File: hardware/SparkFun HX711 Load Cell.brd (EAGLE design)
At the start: 30.5 x 22.9 mm, 25 parts, among them Q1 MMBT4403, U1 HX711

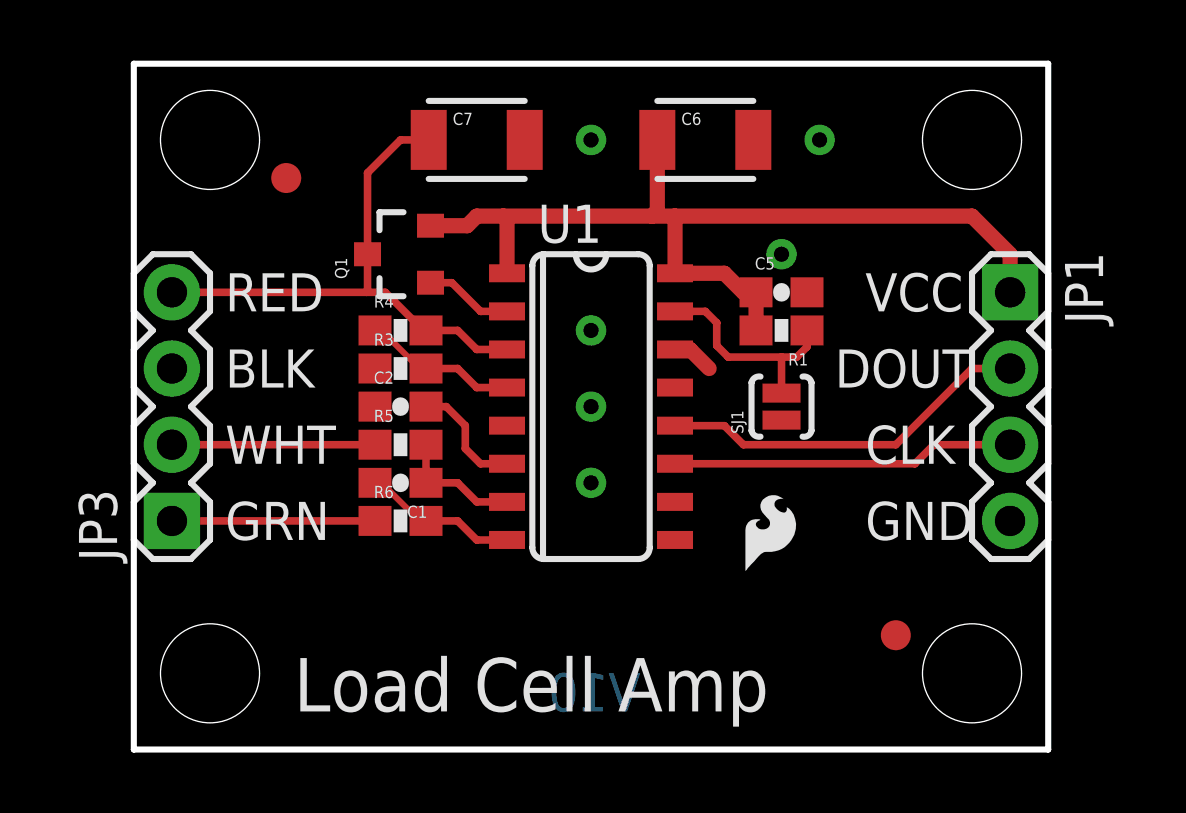
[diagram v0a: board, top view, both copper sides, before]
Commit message: Changes from initial QC checklist. Adding datasheet.
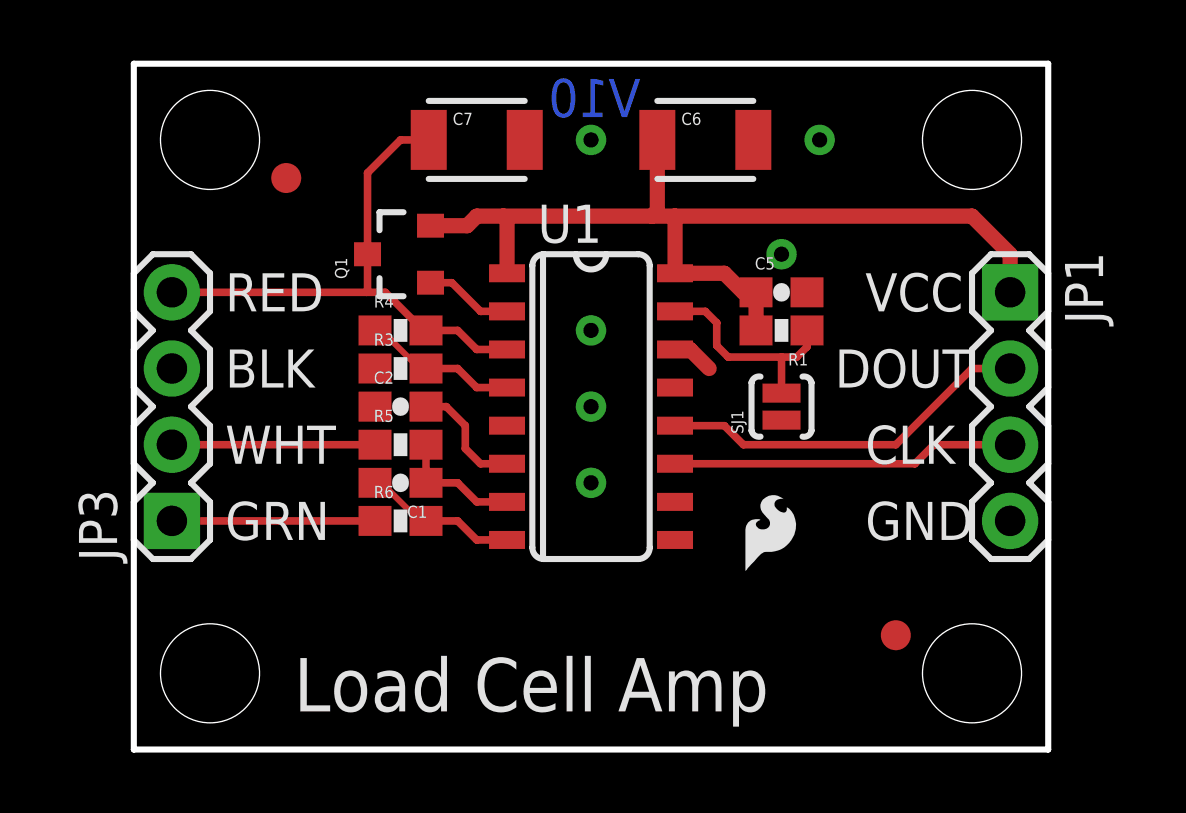
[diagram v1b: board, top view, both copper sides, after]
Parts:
- U1: device HX711:SO16 -> Testing:SO16
- renumbered U$7 to U7
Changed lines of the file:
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@@
 <?xml version="1.0" encoding="utf-8"?>
 <!DOCTYPE eagle SYSTEM "eagle.dtd">
-<eagle version="6.5.0">
+<eagle version="7.1.0">
 <drawing>
 <settings>
@@
 <layer number="251" name="SMDround" color="12" fill="11" visible="no" active="no"/>
 <layer number="254" name="cooling" color="7" fill="1" visible="no" active="yes"/>
+<layer number="255" name="routoute" color="7" fill="1" visible="no" active="yes"/>
 </layers>
 <board>
@@
 <text x="9.398" y="12.065" size="1.27" layer="22" font="vector" ratio="15" rot="MR0">BLK/E-</text>
 <text x="9.398" y="14.605" size="1.27" layer="22" font="vector" ratio="15" rot="MR0">RED/E+</text>
-<text x="16.891" y="1.27" size="1.27" layer="16" font="vector" ratio="20" rot="MR0">V10</text>
+<text x="16.891" y="21.082" size="1.27" layer="16" font="vector" ratio="20" rot="MR0">V10</text>
 <text x="24.384" y="6.985" size="1.27" layer="21" font="vector" ratio="15">GND</text>
 <text x="23.368" y="12.065" size="1.27" layer="21" font="vector" ratio="15">DOUT</text>
@@
 <text x="30.48" y="-21.59" size="1.778" layer="51" font="vector" ratio="15">N. Seidle</text>
 <text x="25.146" y="1.27" size="1.778" layer="22" font="vector" ratio="15" rot="MR0">Load Cell Amp</text>
+<dimension x1="30.48" y1="22.86" x2="0" y2="22.86" x3="15.24" y3="31.75" textsize="1.778" textratio="15" layer="47" unit="inch"/>
+<dimension x1="0" y1="0" x2="0" y2="22.86" x3="-5.08" y3="11.43" textsize="1.778" textratio="15" layer="47" unit="inch"/>
+<dimension x1="27.94" y1="20.32" x2="27.94" y2="2.54" x3="35.56" y3="11.43" textsize="1.778" textratio="15" layer="47" unit="inch"/>
+<dimension x1="27.94" y1="2.54" x2="2.54" y2="2.54" x3="15.24" y3="-5.08" textsize="1.778" textratio="15" layer="47" unit="inch"/>
+<dimension x1="1.27" y1="15.24" x2="29.21" y2="15.24" x3="15.24" y3="27.94" textsize="1.778" textratio="15" layer="47" unit="inch"/>
+<dimension x1="1.27" y1="7.62" x2="1.27" y2="0" x3="-7.62" y3="3.81" textsize="1.778" textratio="15" layer="47" unit="inch"/>
 </plain>
 <attributes>
@@
 <pass name="Default">
 <param name="RoutingGrid" value="50mil"/>
+<param name="AutoGrid" value="1"/>
+<param name="Efforts" value="0"/>
+<param name="TopRouterVariant" value="1"/>
 <param name="tpViaShape" value="round"/>
 <param name="PrefDir.1" value="|"/>
@@
 </autorouter>
 <elements>
-<element name="U$7" library="SparkFun-Aesthetics" package="OSHW-LOGO-S" value="OSHW-LOGOS" x="6.35" y="20.32" rot="MR0"/>
+<element name="U7" library="SparkFun-Aesthetics" package="OSHW-LOGO-S" value="OSHW-LOGOS" x="6.35" y="20.32" rot="MR0"/>
 <element name="FRAME1" library="SparkFun-Aesthetics" package="CREATIVE_COMMONS" value="FRAME-LETTER" x="-0.65105625" y="-21.59"/>
 <element name="STANDOFF1" library="SparkFun-Electromechanical" package="STAND-OFF" value="STAND-OFF" x="2.54" y="2.54"/>
@@
 <element name="LOGO1" library="SparkFun-Aesthetics" package="SFE_LOGO_NAME_FLAME_.1" value="SFE_LOGO_NAME_FLAME.1_INCH" x="21.082" y="4.191" rot="MR0"/>
 <element name="JP1" library="SparkFun-Connectors" package="1X04" value="" x="29.21" y="15.24" rot="R270"/>
-<element name="U1" library="HX711" package="SO16" value="HX711" x="15.24" y="11.43" rot="R270"/>
+<element name="U1" library="Testing" package="SO16" value="HX711" x="15.24" y="11.43" rot="R270">
+<attribute name="PROD_ID" value="IC-12445" x="15.24" y="11.43" size="1.778" layer="27" rot="R270" display="off"/>
+<attribute name="VALUE" value="HX711" x="15.24" y="11.43" size="1.778" layer="27" rot="R270" display="off"/>
+</element>
 <element name="Q1" library="SparkFun-DiscreteSemi" package="SOT23-3" value="MMBT4403" x="8.89" y="16.51" rot="R90">
 <attribute name="PROD_ID" value="TRANS-09245" x="8.89" y="16.51" size="1.778" layer="27" font="vector" ratio="15" rot="R90" display="off"/>

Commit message: Spread out 0603 components and fixed silk. See issue 1.
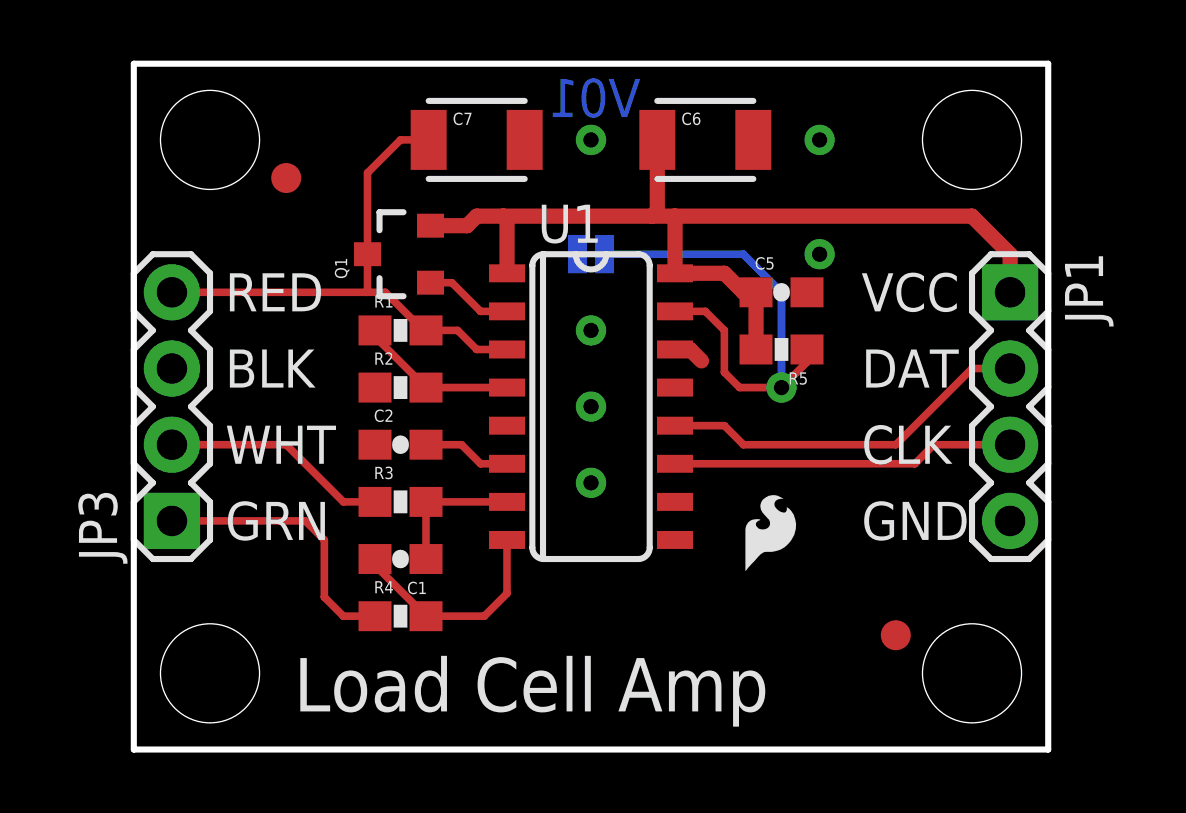
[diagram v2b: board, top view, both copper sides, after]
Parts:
- removed R6: 100, SparkFun-Resistors:0603-RES
- added R2: 10K, SparkFun-Resistors:0603-RES
- R3, R4: value 10K -> 100
- R5: value 100 -> 10K
- moved R5 13.1 mm to (21.6, 13.3), turned to 180 degrees
- moved R1 12.7 mm to (8.89, 14.0), turned to 0 degrees
- moved R4 9.53 mm to (8.89, 4.45)
- moved SJ1 8.13 mm to (15.2, 16.5), flipped to the bottom, turned to 180 degrees
- moved R3 4.44 mm to (8.89, 8.26)
- moved C1 2.54 mm to (8.89, 6.35)
- moved C2 1.27 mm to (8.89, 10.2)
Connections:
- net DOUT renamed DAT
- net A+: now also R4.1; no longer R6.1
- net A-: now also R3.1; no longer R5.1
- net AVDD: now also R1.2; no longer R4.2
- net GND: now also R2.1; no longer R3.1
- net N$1: now also R5.1; no longer R1.1
- net N$2: now also R3.2; no longer R5.2
- net N$3: now also R4.2; no longer R6.2
- net N$6: now also R1.1, R2.2; no longer R3.2, R4.1
- net VCC: now also R5.2; no longer R1.2
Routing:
- net N$1: track 7.37 -> 16.6 mm, vias 0 -> 1
- net A+: track 6.77 -> 9.20 mm
- net N$3: track 5.19 -> 7.41 mm
- net N$7: track 3.94 -> 2.96 mm
- net A-: track 6.77 -> 7.56 mm
- net VCC: track 32.0 -> 32.6 mm
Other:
- board text added: "DAT"
- board text added: "RATE"
- board text added: "V01"
- board text removed: "DOUT"
- board text removed: "V10"

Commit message: Broke out channel B. Adjusted some traces.
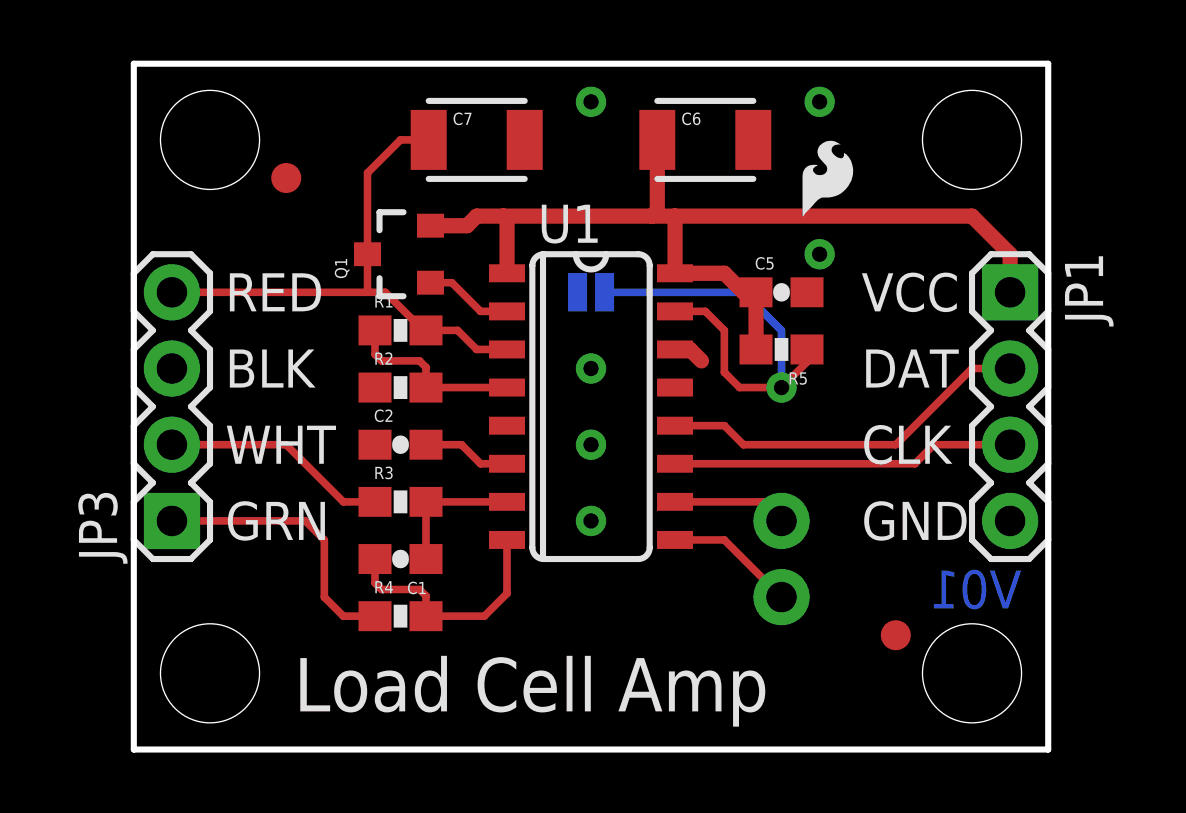
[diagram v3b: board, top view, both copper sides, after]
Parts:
- added JP2: M02PTH, SparkFun-Connectors:1X02
- moved LOGO1 13.0 mm to (21.0, 17.1)
- moved LOGO3 12.0 mm to (22.0, 17.4)
- moved SJ1 1.27 mm to (15.2, 15.2)
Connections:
- new net B+: JP2.1, U1.10
- new net B-: JP2.2, U1.9
- net GND: no longer U1.10, U1.9
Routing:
- net B-: track 0.00 -> 4.34 mm
- net B+: track 0.00 -> 3.81 mm
- net N$1: track 16.6 -> 15.4 mm
- net N$6: track 5.31 -> 6.05 mm
- net N$3: track 7.41 -> 8.15 mm
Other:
- board text added: "B+"
- board text added: "B-"
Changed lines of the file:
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@@
 <?xml version="1.0" encoding="utf-8"?>
 <!DOCTYPE eagle SYSTEM "eagle.dtd">
-<eagle version="6.5.0">
+<eagle version="7.1.0">
 <drawing>
 <settings>
@@
 <layer number="56" name="wert" color="7" fill="1" visible="no" active="no"/>
 <layer number="57" name="tCAD" color="7" fill="1" visible="no" active="no"/>
+<layer number="90" name="Modules" color="5" fill="1" visible="no" active="no"/>
 <layer number="91" name="Nets" color="2" fill="1" visible="no" active="no"/>
 <layer number="92" name="Busses" color="1" fill="1" visible="no" active="no"/>
@@
 <text x="9.398" y="12.065" size="1.27" layer="22" font="vector" ratio="15" rot="MR0">BLK/E-</text>
 <text x="9.398" y="14.605" size="1.27" layer="22" font="vector" ratio="15" rot="MR0">RED/E+</text>
-<text x="16.891" y="21.082" size="1.27" layer="16" font="vector" ratio="20" rot="MR0">V01</text>
+<text x="29.591" y="4.699" size="1.27" layer="16" font="vector" ratio="20" rot="MR0">V01</text>
 <text x="24.257" y="6.985" size="1.27" layer="21" font="vector" ratio="15">GND</text>
 <text x="24.257" y="12.065" size="1.27" layer="21" font="vector" ratio="15">DAT</text>
@@
 <dimension x1="1.27" y1="15.24" x2="29.21" y2="15.24" x3="15.24" y3="27.94" textsize="1.778" textratio="15" layer="47" unit="inch"/>
 <dimension x1="1.27" y1="7.62" x2="1.27" y2="0" x3="-7.62" y3="3.81" textsize="1.778" textratio="15" layer="47" unit="inch"/>
-<text x="20.955" y="15.875" size="1.27" layer="22" font="vector" ratio="15" rot="MR0">RATE</text>
+<text x="20.955" y="14.605" size="1.27" layer="22" font="vector" ratio="15" rot="MR0">RATE</text>
+<text x="19.685" y="6.985" size="1.27" layer="22" font="vector" ratio="15" rot="MR0">B+</text>
+<text x="19.685" y="4.445" size="1.27" layer="22" font="vector" ratio="15" rot="MR0">B-</text>
 </plain>
 <attributes>
@@
 <pass name="Default">
 <param name="RoutingGrid" value="50mil"/>
+<param name="AutoGrid" value="1"/>
+<param name="Efforts" value="0"/>
+<param name="TopRouterVariant" value="1"/>
 <param name="tpViaShape" value="round"/>
 <param name="PrefDir.1" value="|"/>
@@
 <element name="STANDOFF3" library="SparkFun-Electromechanical" package="STAND-OFF" value="STAND-OFF" x="2.54" y="20.32"/>
 <element name="STANDOFF4" library="SparkFun-Electromechanical" package="STAND-OFF" value="STAND-OFF" x="27.94" y="20.32"/>
-<element name="LOGO1" library="SparkFun-Aesthetics" package="SFE_LOGO_NAME_FLAME_.1" value="SFE_LOGO_NAME_FLAME.1_INCH" x="21.082" y="4.191" rot="MR0"/>
+<element name="LOGO1" library="SparkFun-Aesthetics" package="SFE_LOGO_NAME_FLAME_.1" value="SFE_LOGO_NAME_FLAME.1_INCH" x="20.955" y="17.145" rot="MR0"/>
 <element name="JP1" library="SparkFun-Connectors" package="1X04" value="" x="29.21" y="15.24" rot="R270"/>
 <element name="U1" library="Testing" package="SO16" value="HX711" x="15.24" y="11.43" rot="R270">
@@
 <attribute name="PROD_ID" value="RES-00824" x="21.59" y="13.335" size="1.778" layer="27" font="vector" ratio="15" rot="R180" display="off"/>
 </element>
-<element name="SJ1" library="SparkFun-Passives" package="PAD-JUMPER-2-NO_YES_SILK" value="" x="15.24" y="16.51" rot="MR180"/>
+<element name="SJ1" library="SparkFun-Passives" package="PAD-JUMPER-2-NO_YES_SILK" value="" x="15.24" y="15.24" rot="MR180"/>
 <element name="C1" library="SparkFun-Capacitors" package="0603-CAP" value="0.1uF" x="8.89" y="6.35" rot="R180">
 <attribute name="PROD_ID" value="CAP-08604" x="8.89" y="6.35" size="1.778" layer="27" font="vector" ratio="15" rot="R180" display="off"/>
@@
 <attribute name="PROD_ID" value="CAP-08604" x="8.89" y="10.16" size="1.778" layer="27" font="vector" ratio="15" display="off"/>
 </element>
-<element name="LOGO3" library="SparkFun-Aesthetics" package="SFE_LOGO_FLAME_.1" value="SFE_LOGO_FLAME.1_INCH" x="20.066" y="5.588"/>
+<element name="LOGO3" library="SparkFun-Aesthetics" package="SFE_LOGO_FLAME_.1" value="SFE_LOGO_FLAME.1_INCH" x="21.971" y="17.399"/>
 <element name="FID1" library="SparkFun-Aesthetics" package="FIDUCIAL-1X2" value="FIDUCIAL1X2" x="5.08" y="19.05"/>
 <element name="FID2" library="SparkFun-Aesthetics" package="FIDUCIAL-1X2" value="FIDUCIAL1X2" x="25.4" y="3.81"/>
+<element name="JP2" library="SparkFun-Connectors" package="1X02" value="M02PTH" x="21.59" y="7.62" rot="MR270"/>
 </elements>
 <signals>
@@
 <contactref element="R2" pad="1"/>
 <contactref element="JP3" pad="3"/>
-<contactref element="U1" pad="9"/>
-<contactref element="U1" pad="10"/>
 <contactref element="SJ1" pad="1"/>
 <contactref element="C2" pad="1"/>
 <contactref element="C5" pad="2"/>
 <via x="22.86" y="16.51" extent="1-16" drill="0.508"/>
-<via x="22.86" y="20.32" extent="1-16" drill="0.508"/>
-<via x="15.24" y="13.97" extent="1-16" drill="0.508"/>
-<via x="15.24" y="11.43" extent="1-16" drill="0.508"/>
-<via x="15.24" y="8.89" extent="1-16" drill="0.508"/>
-<via x="15.24" y="20.32" extent="1-16" drill="0.508"/>
+<via x="22.86" y="21.59" extent="1-16" drill="0.508"/>
+<via x="15.24" y="12.7" extent="1-16" drill="0.508"/>
+<via x="15.24" y="10.16" extent="1-16" drill="0.508"/>
+<via x="15.24" y="7.62" extent="1-16" drill="0.508"/>
+<via x="15.24" y="21.59" extent="1-16" drill="0.508"/>
 <wire x1="18.288" y1="13.335" x2="18.542" y2="13.335" width="0.508" layer="1"/>
 <wire x1="18.542" y1="13.335" x2="18.923" y2="12.954" width="0.508" layer="1"/>
@@
 <contactref element="R1" pad="1"/>
 <wire x1="12.44" y1="12.065" x2="9.74" y2="12.065" width="0.254" layer="1"/>
-<wire x1="8.04" y1="13.97" x2="8.04" y2="13.765" width="0.254" layer="1"/>
-<wire x1="8.04" y1="13.765" x2="9.74" y2="12.065" width="0.254" layer="1"/>
+<wire x1="8.04" y1="13.97" x2="8.04" y2="13.169" width="0.254" layer="1"/>
+<wire x1="8.04" y1="13.169" x2="8.255" y2="12.954" width="0.254" layer="1"/>
+<wire x1="8.255" y1="12.954" x2="9.525" y2="12.954" width="0.254" layer="1"/>
+<wire x1="9.525" y1="12.954" x2="9.74" y2="12.739" width="0.254" layer="1"/>
+<wire x1="9.74" y1="12.065" x2="9.74" y2="12.739" width="0.254" layer="1"/>
 </signal>
 <signal name="N$7">
@@
 <wire x1="18.04" y1="14.605" x2="19.05" y2="14.605" width="0.254" layer="1"/>
 <via x="21.59" y="12.065" extent="1-16" drill="0.508"/>
-<wire x1="15.69" y1="16.51" x2="20.32" y2="16.51" width="0.254" layer="16"/>
-<wire x1="20.32" y1="16.51" x2="21.59" y2="15.24" width="0.254" layer="16"/>
-<wire x1="21.59" y1="15.24" x2="21.59" y2="12.065" width="0.254" layer="16"/>
+<wire x1="15.69" y1="15.24" x2="20.32" y2="15.24" width="0.254" layer="16"/>
+<wire x1="20.32" y1="15.24" x2="21.59" y2="13.97" width="0.254" layer="16"/>
+<wire x1="21.59" y1="13.97" x2="21.59" y2="12.065" width="0.254" layer="16"/>
 <wire x1="22.44" y1="13.335" x2="22.44" y2="12.915" width="0.254" layer="1"/>
 <wire x1="22.44" y1="12.915" x2="21.59" y2="12.065" width="0.254" layer="1"/>
@@
 <wire x1="12.44" y1="5.201" x2="11.684" y2="4.445" width="0.254" layer="1"/>
 <wire x1="11.684" y1="4.445" x2="9.74" y2="4.445" width="0.254" layer="1"/>
-<wire x1="8.04" y1="6.35" x2="8.04" y2="6.145" width="0.254" layer="1"/>
-<wire x1="8.04" y1="6.145" x2="9.74" y2="4.445" width="0.254" layer="1"/>
+<wire x1="8.04" y1="6.35" x2="8.04" y2="5.549" width="0.254" layer="1"/>
+<wire x1="8.04" y1="5.549" x2="8.255" y2="5.334" width="0.254" layer="1"/>
+<wire x1="8.255" y1="5.334" x2="9.525" y2="5.334" width="0.254" layer="1"/>
+<wire x1="9.525" y1="5.334" x2="9.74" y2="5.119" width="0.254" layer="1"/>
+<wire x1="9.74" y1="4.445" x2="9.74" y2="5.119" width="0.254" layer="1"/>
 </signal>
 <signal name="A-">
@@
 <wire x1="5.715" y1="7.62" x2="1.27" y2="7.62" width="0.254" layer="1"/>
 </signal>
+<signal name="B+">
+<contactref element="U1" pad="10"/>
+<contactref element="JP2" pad="1"/>
+<wire x1="18.04" y1="8.255" x2="20.955" y2="8.255" width="0.254" layer="1"/>
+<wire x1="20.955" y1="8.255" x2="21.59" y2="7.62" width="0.254" layer="1"/>
+</signal>
+<signal name="B-">
+<contactref element="U1" pad="9"/>
+<contactref element="JP2" pad="2"/>
+<wire x1="18.04" y1="6.985" x2="19.685" y2="6.985" width="0.254" layer="1"/>
+<wire x1="19.685" y1="6.985" x2="21.59" y2="5.08" width="0.254" layer="1"/>
+</signal>
 </signals>
